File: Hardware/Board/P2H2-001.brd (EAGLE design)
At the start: 45 x 45 mm, 18 parts, among them K1 G5V1, T1 2SC1815

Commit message: Fixed connection error of MIDI IN.
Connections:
- net N$12: now also OK1.6; no longer OK1.5
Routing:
- net N$12: track 44.4 -> 42.3 mm
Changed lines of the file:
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@@
 </signal>
 <signal name="N$12">
-<contactref element="OK1" pad="5"/>
 <contactref element="U$1" pad="2"/>
-<wire x1="14.1732" y1="35.433" x2="15.0876" y2="35.433" width="0.254" layer="1"/>
-<wire x1="7.7724" y1="29.0322" x2="14.1732" y2="35.433" width="0.254" layer="1"/>
-<wire x1="6.858" y1="29.0322" x2="7.7724" y2="29.0322" width="0.254" layer="1"/>
-<wire x1="4.1148" y1="26.289" x2="6.858" y2="29.0322" width="0.254" layer="1"/>
+<contactref element="OK1" pad="6"/>
+<wire x1="12.573" y1="34.7472" x2="12.573" y2="35.433" width="0.254" layer="1"/>
+<wire x1="4.1148" y1="26.289" x2="12.573" y2="34.7472" width="0.254" layer="1"/>
 <wire x1="1.8288" y1="26.289" x2="4.1148" y2="26.289" width="0.254" layer="1"/>
 <wire x1="1.143" y1="25.6032" x2="1.8288" y2="26.289" width="0.254" layer="1"/>
@@
 <wire x1="10.9728" y1="7.0866" x2="8.001" y2="7.0866" width="0.254" layer="1"/>
 <wire x1="12.1158" y1="8.2296" x2="10.9728" y2="7.0866" width="0.254" layer="1"/>
-<wire x1="15.0876" y1="35.433" x2="15.24" y2="35.56" width="0.254" layer="1"/>
+<wire x1="12.573" y1="35.433" x2="12.7" y2="35.56" width="0.254" layer="1"/>
 <wire x1="12.1158" y1="8.2296" x2="12.34" y2="8.38" width="0.254" layer="1"/>
 </signal>

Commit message: Adopted to Relayport.
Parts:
- JP3: device pinhead:1X02 -> pinhead:1X04
- R3: value 120 -> 220
- turned R3 to 180 degrees
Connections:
- removed net N$1: CN1.3, R3.2
- removed net N$2: CN1.4, R3.1
- new net N$10: JP3.1, R3.1
- net GND: now also JP3.2
- net N$18: now also JP3.3; no longer JP3.1
- net N$19: now also JP3.4; no longer JP3.2
- net VCC: now also R3.2
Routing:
- net N$10: track 0.00 -> 26.2 mm
- net GND: track 124.9 -> 143.5 mm
- net N$1: track 12.5 -> 0.00 mm
- net VCC: track 61.3 -> 68.5 mm
- net N$2: track 4.53 -> 0.00 mm
- net N$18: track 8.40 -> 5.89 mm
- net N$19: track 17.9 -> 16.8 mm

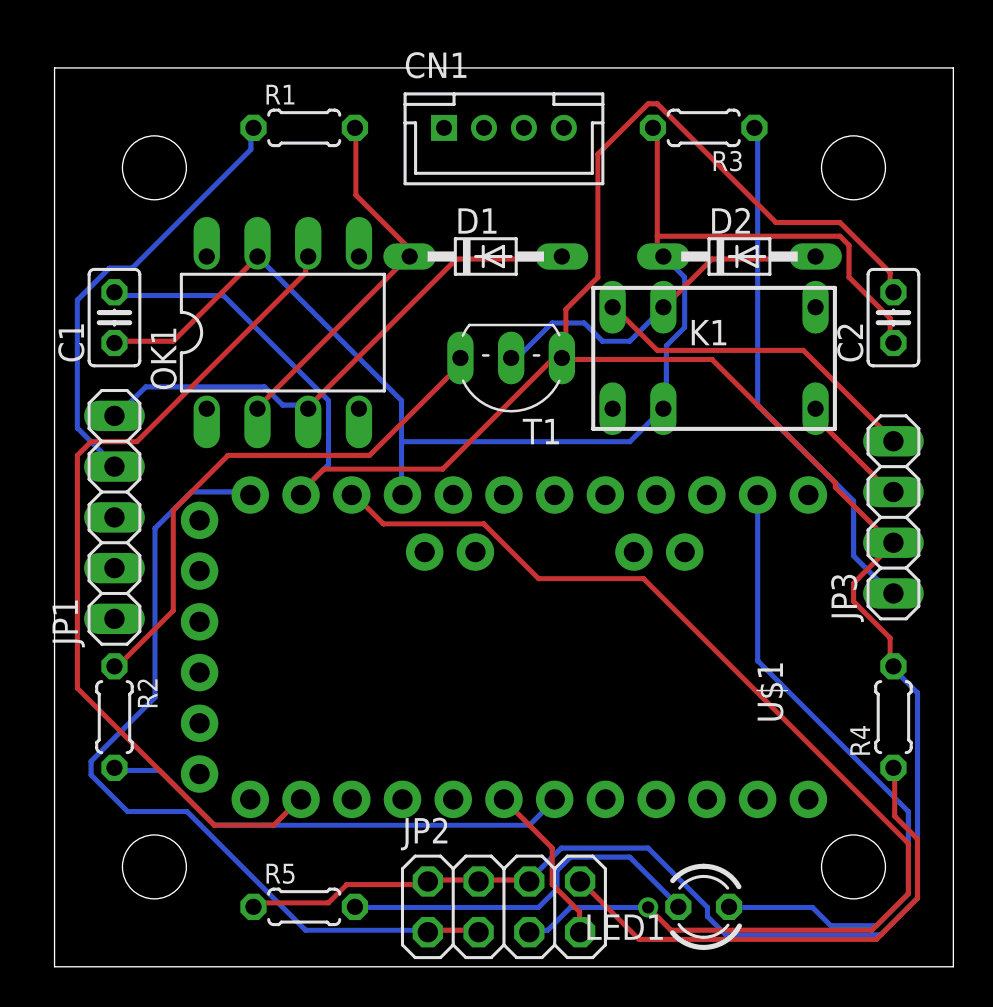
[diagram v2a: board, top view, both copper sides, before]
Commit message: Changed layout of ZeroVoltage.
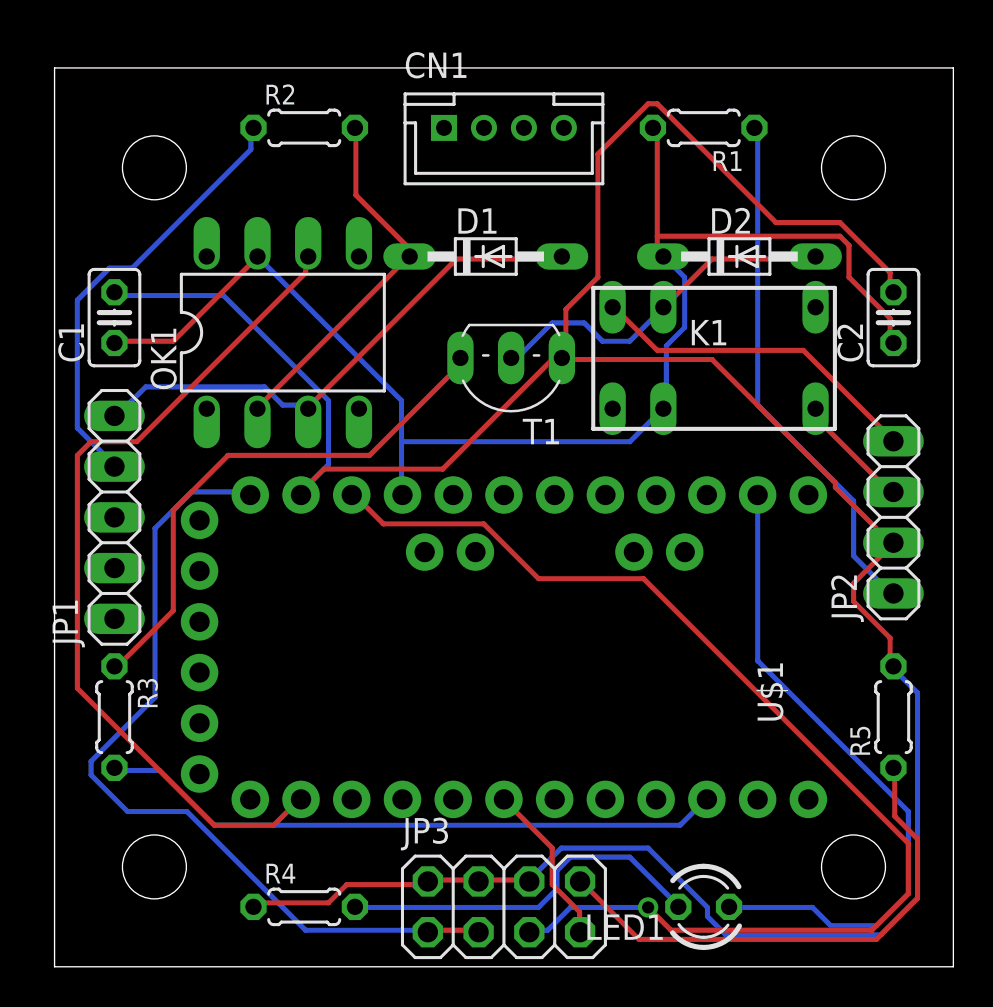
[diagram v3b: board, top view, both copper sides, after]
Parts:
- JP2: device pinhead:2X04 -> pinhead:1X04
- JP3: device pinhead:1X04 -> pinhead:2X04
- R2: value 3.3k -> 220
- R3: value 220 -> 3.3k
- R4: value 220 -> 330
- R5: value 330 -> 150
- moved R3 41.7 mm to (3.00, 12.5), turned to 270 degrees
- moved R2 31.0 mm to (12.5, 42.0), turned to 0 degrees
- moved R4 31.0 mm to (12.5, 3.00), turned to 0 degrees
- moved R5 31.0 mm to (42.0, 12.5), turned to 90 degrees
- moved JP2 27.6 mm to (42.0, 22.5), turned to 90 degrees
- moved JP3 27.6 mm to (22.5, 3.00), turned to 0 degrees
- moved R1 20.0 mm to (32.5, 42.0), turned to 180 degrees
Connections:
- removed net N$14: R2.2, U$1.7
- new net N$1: R3.2, U$1.10
- net GND: now also JP3.4, JP3.6, R4.1, R5.2; no longer JP2.4, JP2.6, R4.2, R5.1
- net N$10: now also JP2.1, R1.1; no longer JP3.1, R3.1
- net N$13: now also R3.1; no longer R2.1
- net N$17: now also R4.2; no longer R5.2
- net N$18: now also JP2.3; no longer JP3.3
- net N$19: now also JP2.4; no longer JP3.4
- net N$3: now also R2.1; no longer R1.1
- net N$4: now also R2.2; no longer R1.2
- net N$5: now also JP3.8, R5.1; no longer JP2.8, R4.1
- net N$6: now also JP3.5; no longer JP2.5
- net N$8: now also JP3.7; no longer JP2.7
- net N$9: now also JP3.1, JP3.3; no longer JP2.1, JP2.3
- net VCC: now also R1.2; no longer R3.2
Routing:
- net N$1: track 0.00 -> 31.4 mm
- net N$14: track 23.8 -> 0.00 mm
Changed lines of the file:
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@@
 <element name="C1" library="rcl" package="C025-025X050" value="104" x="3" y="32.5" rot="R90"/>
 <element name="C2" library="rcl" package="C025-025X050" value="103" x="42" y="32.5" rot="R90"/>
-<element name="R1" library="resistor" package="0204/5" value="220" x="12.5" y="42"/>
+<element name="R2" library="resistor" package="0204/5" value="220" x="12.5" y="42"/>
 <element name="JP1" library="pinhead" package="1X05" value="" x="3" y="22.5" rot="R90"/>
-<element name="JP2" library="pinhead" package="2X04" value="" x="22.5" y="3"/>
-<element name="R4" library="resistor" package="0204/5" value="220" x="42" y="12.5" rot="R90"/>
-<element name="R3" library="resistor" package="0204/5" value="220" x="32.5" y="42" rot="R180"/>
+<element name="JP3" library="pinhead" package="2X04" value="" x="22.5" y="3"/>
+<element name="R5" library="resistor" package="0204/5" value="150" x="42" y="12.5" rot="R90"/>
+<element name="R1" library="resistor" package="0204/5" value="220" x="32.5" y="42" rot="R180"/>
 <element name="CN1" library="jst-ph" package="B4B-PH-K-S" value="" x="22.5" y="42"/>
-<element name="U$1" library="SparkFun-Boards" package="ARDUINO_PRO_MINI" value="ARDUINO_PRO_MINI" x="22.5" y="16" rot="R90"/>
-<element name="R5" library="resistor" package="0204/5" value="330" x="12.5" y="3"/>
+<element name="R4" library="resistor" package="0204/5" value="330" x="12.5" y="3"/>
 <element name="LED1" library="led" package="LED3MM" value="" x="32.5" y="3" rot="R180"/>
 <element name="T1" library="transistor" package="TO92-ECB" value="2SC1815" x="22.86" y="30.48" rot="R180"/>
@@
 <element name="D1" library="diode" package="DO34-7" value="BAS15" x="21.59" y="35.56"/>
 <element name="D2" library="diode" package="DO34-7" value="BAS15" x="34.29" y="35.56"/>
-<element name="R2" library="resistor" package="0204/5" value="3.3k" x="3" y="12.5" rot="R270"/>
-<element name="JP3" library="pinhead" package="1X04" value="" x="42" y="22.5" rot="R90"/>
+<element name="R3" library="resistor" package="0204/5" value="3.3k" x="3" y="12.5" rot="R270"/>
+<element name="JP2" library="pinhead" package="1X04" value="" x="42" y="22.5" rot="R90"/>
+<element name="U$1" library="SparkFun-Boards" package="ARDUINO_PRO_MINI" value="ARDUINO_PRO_MINI" x="22.5" y="16" rot="R90"/>
 </elements>
 <signals>
@@
 <contactref element="C1" pad="2"/>
 <contactref element="C2" pad="2"/>
+<contactref element="JP3" pad="2"/>
+<contactref element="JP3" pad="4"/>
+<contactref element="JP3" pad="6"/>
+<contactref element="R5" pad="2"/>
+<contactref element="T1" pad="E"/>
+<contactref element="R4" pad="1"/>
 <contactref element="JP2" pad="2"/>
-<contactref element="JP2" pad="4"/>
-<contactref element="JP2" pad="6"/>
-<contactref element="R4" pad="2"/>
 <contactref element="U$1" pad="23"/>
-<contactref element="T1" pad="E"/>
-<contactref element="R5" pad="1"/>
-<contactref element="JP3" pad="2"/>
 <wire x1="23.5458" y1="4.3434" x2="21.2598" y2="4.3434" width="0.254" layer="1"/>
 <wire x1="21.2598" y1="4.3434" x2="21.23" y2="4.27" width="0.254" layer="1"/>
@@
 <contactref element="C2" pad="1"/>
 <contactref element="C1" pad="1"/>
-<contactref element="U$1" pad="21"/>
 <contactref element="OK1" pad="7"/>
 <contactref element="K1" pad="2"/>
 <contactref element="D2" pad="C"/>
-<contactref element="R3" pad="2"/>
+<contactref element="R1" pad="2"/>
+<contactref element="U$1" pad="21"/>
 <wire x1="30.6324" y1="31.0896" x2="30.6324" y2="28.1178" width="0.254" layer="16"/>
 <wire x1="31.5468" y1="32.004" x2="30.6324" y2="31.0896" width="0.254" layer="16"/>
@@
 </signal>
 <signal name="N$5">
-<contactref element="R4" pad="1"/>
-<contactref element="JP2" pad="8"/>
+<contactref element="R5" pad="1"/>
+<contactref element="JP3" pad="8"/>
 <wire x1="42.0624" y1="7.5438" x2="42.0624" y2="9.8298" width="0.254" layer="1"/>
 <wire x1="43.2054" y1="6.4008" x2="42.0624" y2="7.5438" width="0.254" layer="1"/>
@@
 </signal>
 <signal name="N$6">
-<contactref element="JP2" pad="5"/>
+<contactref element="JP3" pad="5"/>
 <contactref element="U$1" pad="22"/>
 <wire x1="24.6888" y1="1.8288" x2="23.7744" y2="1.8288" width="0.254" layer="16"/>
@@
 </signal>
 <signal name="N$8">
-<contactref element="JP2" pad="7"/>
+<contactref element="JP3" pad="7"/>
 <contactref element="U$1" pad="6"/>
 <wire x1="26.289" y1="2.7432" x2="26.289" y2="1.8288" width="0.254" layer="1"/>
@@
 </signal>
 <signal name="N$9">
-<contactref element="JP2" pad="3"/>
-<contactref element="JP2" pad="1"/>
+<contactref element="JP3" pad="3"/>
+<contactref element="JP3" pad="1"/>
 <contactref element="U$1" pad="24"/>
 <wire x1="21.0312" y1="1.8288" x2="18.7452" y2="1.8288" width="0.254" layer="1"/>
@@
 </signal>
 <signal name="N$3">
-<contactref element="R1" pad="1"/>
+<contactref element="R2" pad="1"/>
 <contactref element="JP1" pad="4"/>
 <wire x1="9.8298" y1="40.9194" x2="9.8298" y2="41.8338" width="0.254" layer="16"/>
@@
 </signal>
 <signal name="N$4">
-<contactref element="R1" pad="2"/>
+<contactref element="R2" pad="2"/>
 <contactref element="OK1" pad="2"/>
 <contactref element="D1" pad="C"/>
@@
 </signal>
 <signal name="N$12">
+<contactref element="OK1" pad="6"/>
 <contactref element="U$1" pad="2"/>
-<contactref element="OK1" pad="6"/>
 <wire x1="12.573" y1="34.7472" x2="12.573" y2="35.433" width="0.254" layer="1"/>
 <wire x1="4.1148" y1="26.289" x2="12.573" y2="34.7472" width="0.254" layer="1"/>
@@
 <signal name="N$18">
 <contactref element="K1" pad="5"/>
-<contactref element="JP3" pad="3"/>
+<contactref element="JP2" pad="3"/>
 <wire x1="38.1762" y1="27.432" x2="38.1762" y2="27.8892" width="0.254" layer="1"/>
 <wire x1="41.8338" y1="23.7744" x2="38.1762" y2="27.432" width="0.254" layer="1"/>
@@
 <signal name="N$19">
 <contactref element="K1" pad="10"/>
-<contactref element="JP3" pad="4"/>
+<contactref element="JP2" pad="4"/>
 <wire x1="30.1752" y1="30.861" x2="28.1178" y2="32.9184" width="0.254" layer="1"/>
 <wire x1="37.4904" y1="30.861" x2="30.1752" y2="30.861" width="0.254" layer="1"/>
@@
 </signal>
 <signal name="N$16">
+<contactref element="LED1" pad="A"/>
 <contactref element="U$1" pad="14"/>
-<contactref element="LED1" pad="A"/>
 <wire x1="37.9476" y1="2.9718" x2="33.8328" y2="2.9718" width="0.254" layer="16"/>
 <wire x1="38.862" y1="2.0574" x2="37.9476" y2="2.9718" width="0.254" layer="16"/>
@@
 <signal name="N$17">
 <contactref element="LED1" pad="K"/>
-<contactref element="R5" pad="2"/>
+<contactref element="R4" pad="2"/>
 <wire x1="24.2316" y1="2.9718" x2="15.0876" y2="2.9718" width="0.254" layer="16"/>
 <wire x1="25.146" y1="3.8862" x2="24.2316" y2="2.9718" width="0.254" layer="16"/>
@@
 <signal name="N$13">
 <contactref element="T1" pad="B"/>
-<contactref element="R2" pad="1"/>
+<contactref element="R3" pad="1"/>
 <wire x1="5.9436" y1="17.8308" x2="3.2004" y2="15.0876" width="0.254" layer="1"/>
 <wire x1="5.9436" y1="22.86" x2="5.9436" y2="17.8308" width="0.254" layer="1"/>
@@
 <wire x1="20.1168" y1="30.4038" x2="20.32" y2="30.48" width="0.254" layer="1"/>
 </signal>
-<signal name="N$14">
-<contactref element="R2" pad="2"/>
-<contactref element="U$1" pad="7"/>
-<wire x1="5.2578" y1="9.8298" x2="3.2004" y2="9.8298" width="0.254" layer="16"/>
-<wire x1="8.001" y1="7.0866" x2="5.2578" y2="9.8298" width="0.254" layer="16"/>
-<wire x1="23.7744" y1="7.0866" x2="8.001" y2="7.0866" width="0.254" layer="16"/>
-<wire x1="24.9174" y1="8.2296" x2="23.7744" y2="7.0866" width="0.254" layer="16"/>
-<wire x1="3.2004" y1="9.8298" x2="3" y2="9.96" width="0.254" layer="16"/>
-<wire x1="24.9174" y1="8.2296" x2="25.04" y2="8.38" width="0.254" layer="16"/>
-</signal>
 <signal name="N$10">
-<contactref element="JP3" pad="1"/>
-<contactref element="R3" pad="1"/>
+<contactref element="JP2" pad="1"/>
+<contactref element="R1" pad="1"/>
 <wire x1="35.2044" y1="28.1178" x2="35.2044" y2="41.8338" width="0.254" layer="16"/>
 <wire x1="40.005" y1="23.3172" x2="35.2044" y2="28.1178" width="0.254" layer="16"/>
@@
 <wire x1="41.8338" y1="18.7452" x2="42" y2="18.69" width="0.254" layer="16"/>
 </signal>
+<signal name="N$1">
+<contactref element="R3" pad="2"/>
+<contactref element="U$1" pad="10"/>
+<wire x1="5.2578" y1="9.8298" x2="3.2004" y2="9.8298" width="0.254" layer="16"/>
+<wire x1="8.001" y1="7.0866" x2="5.2578" y2="9.8298" width="0.254" layer="16"/>
+<wire x1="31.3182" y1="7.0866" x2="8.001" y2="7.0866" width="0.254" layer="16"/>
+<wire x1="32.4612" y1="8.2296" x2="31.3182" y2="7.0866" width="0.254" layer="16"/>
+<wire x1="3.2004" y1="9.8298" x2="3" y2="9.96" width="0.254" layer="16"/>
+<wire x1="32.4612" y1="8.2296" x2="32.66" y2="8.38" width="0.254" layer="16"/>
+</signal>
 </signals>

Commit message: Merged H2 and H3.
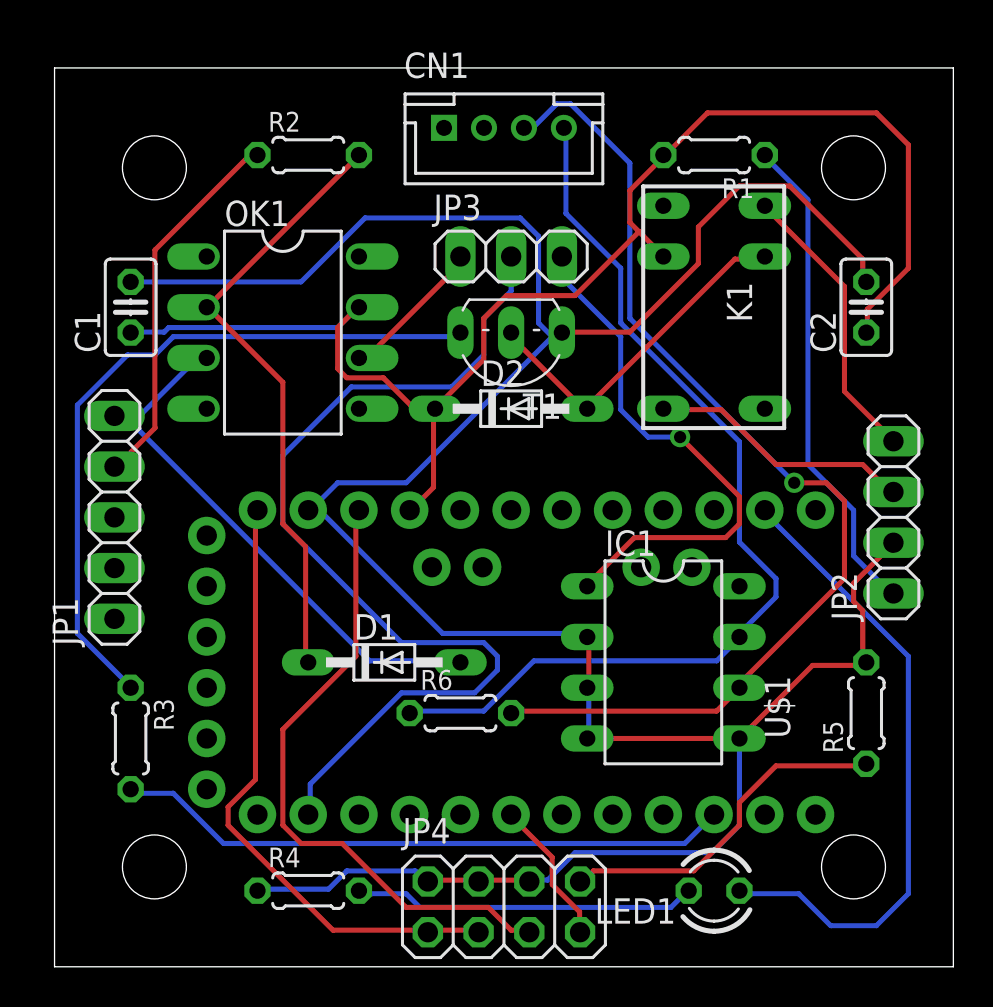
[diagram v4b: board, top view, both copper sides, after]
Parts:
- added IC1: LTC485N, linear-technology:DIL08
- added JP4: (no value), pinhead:2X04
- added R6: 120, resistor:0204/5
- JP3: device pinhead:2X04 -> pinhead:1X03
- moved JP3 32.6 mm to (22.9, 35.6)
- moved D1 20.9 mm to (16.5, 15.2)
- moved D2 13.7 mm to (22.9, 27.9)
- moved K1 2.54 mm to (33.0, 33.0), turned to 270 degrees
- moved C2 1.46 mm to (40.6, 33.0)
- moved R1 1.46 mm to (33.0, 40.6)
- moved R2 1.37 mm to (12.7, 40.6)
- moved R5 1.37 mm to (40.6, 12.7)
- moved R3 1.34 mm to (3.81, 11.4)
- moved T1 1.27 mm to (22.9, 31.8)
- moved C1 0.96 mm to (3.81, 33.0)
- moved LED1 0.96 mm to (33.0, 3.81)
- moved U$1 0.84 mm to (22.9, 15.2)
- moved R4 0.83 mm to (12.7, 3.81)
- turned OK1 to 270 degrees
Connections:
- new net N$11: CN1.4, IC1.7, R6.1
- new net N$14: IC1.1, JP3.3
- new net N$2: CN1.3, IC1.6, R6.2
- new net N$20: JP3.2, U$1.2
- net GND: now also IC1.2, IC1.3, IC1.4, IC1.5, JP4.2, JP4.4, JP4.6; no longer JP3.2, JP3.4, JP3.6
- net N$12: now also JP3.1; no longer U$1.2
- net N$5: now also JP4.8; no longer JP3.8
- net N$6: now also JP4.5; no longer JP3.5
- net N$8: now also JP4.7; no longer JP3.7
- net N$9: now also JP4.1, JP4.3; no longer JP3.1, JP3.3
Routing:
- net N$2: track 0.00 -> 52.9 mm, vias 0 -> 1
- net N$11: track 0.00 -> 48.8 mm
- net N$20: track 0.00 -> 48.5 mm
- net N$12: track 42.3 -> 7.47 mm
- net N$14: track 0.00 -> 27.0 mm, vias 0 -> 1
- net N$6: track 58.4 -> 32.0 mm, vias 1 -> 0
- net N$4: track 18.4 -> 30.7 mm
- net N$9: track 42.0 -> 31.3 mm
- net N$13: track 26.9 -> 35.9 mm
- net N$5: track 26.0 -> 17.4 mm
- net N$18: track 5.89 -> 13.2 mm
- net VCC: track 68.5 -> 72.5 mm
- net N$3: track 22.0 -> 18.9 mm
- net N$19: track 16.8 -> 14.4 mm
- net GND: track 143.5 -> 141.5 mm
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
